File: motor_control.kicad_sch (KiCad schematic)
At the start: 9 parts, among them M1 Motor_DC, M2 Motor_DC, Q3 NJFET, U2 DRV8833PWP

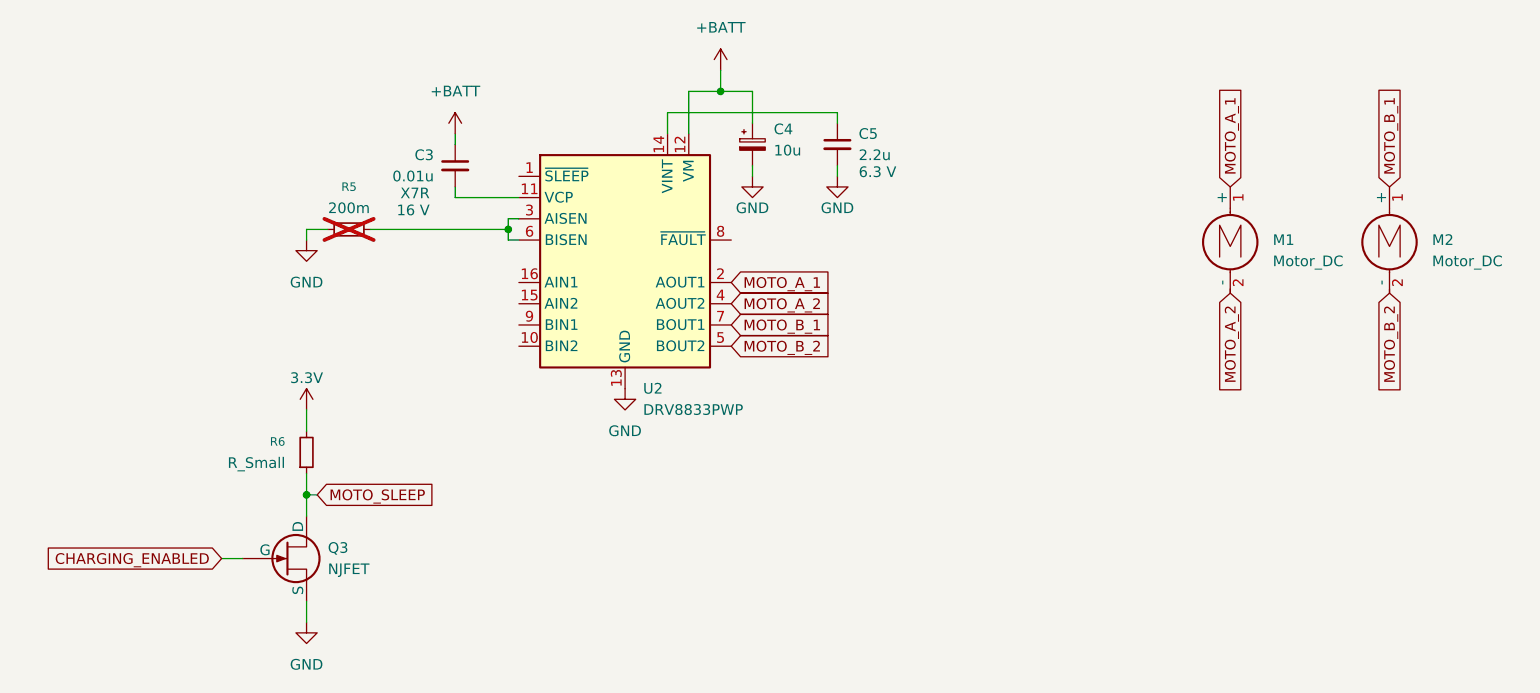
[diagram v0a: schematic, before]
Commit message: Finalized charger detection circuit, designed voltage monitor circuit, added pogo connector, finalized motor driver connections, added ESP32 connections
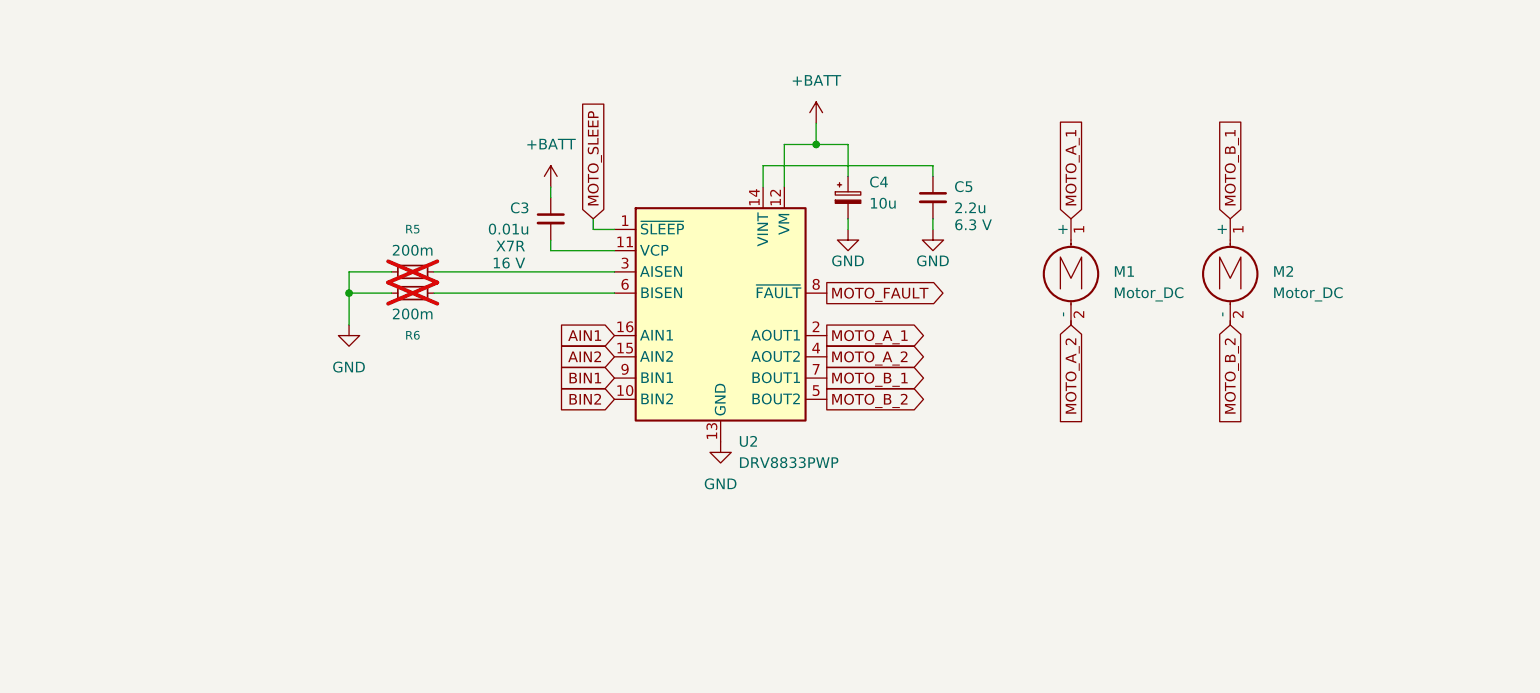
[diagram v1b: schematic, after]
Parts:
- removed Q3: NJFET, symbol Simulation_SPICE:NJFET
- R6: value R_Small -> 200m; now not fitted
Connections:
- net 3.3V is gone; now on net GND: R6.2
- net MOTO_SLEEP: now also U2.1 (~{SLEEP}); no longer R6.1
- net at R5.2, U2.3 (AISEN): no longer U2.6 (BISEN)
- net BIN2: now reaches U2.10 (BIN2)
- net AIN2: now reaches U2.15 (AIN2)
- net AIN1: now reaches U2.16 (AIN1)
- net MOTO_FAULT: now reaches U2.8 (~{FAULT})
- net BIN1: now reaches U2.9 (BIN1)
- new net: R6.1, U2.6 (BISEN)
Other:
- moved on the sheet: C3, C4, C5, M1, M2, R5, U2

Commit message: Assigned footprints, new pogo footprint, added test points
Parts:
- added TP10, TP11, TP12, TP13, TP14, TP7, TP8, TP9: TestPoint_Small, TestPoint:TestPoint_Pad_D1.0mm, symbol Connector:TestPoint_Small
- C3, C4, C5: footprint (none) -> Capacitor_SMD:C_1206_3216Metric_Pad1.33x1.80mm_HandSolder
- R5, R6: footprint (none) -> Resistor_SMD:R_1206_3216Metric_Pad1.30x1.75mm_HandSolder
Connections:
- net AIN1: now also TP7.1
- net AIN2: now also TP8.1
- net BIN1: now also TP9.1
- net BIN2: now also TP10.1
- net MOTO_A_1: now also TP11.1
- net MOTO_A_2: now also TP12.1
- net MOTO_B_1: now also TP13.1
- net MOTO_B_2: now also TP14.1
